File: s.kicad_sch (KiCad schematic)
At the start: 16 parts, among them J1 USB4085-GF-A_REVB, J2 UART connector, SW26 210-4MS, U1 ESP32-S3-WROOM-1, U2 MCP1825S

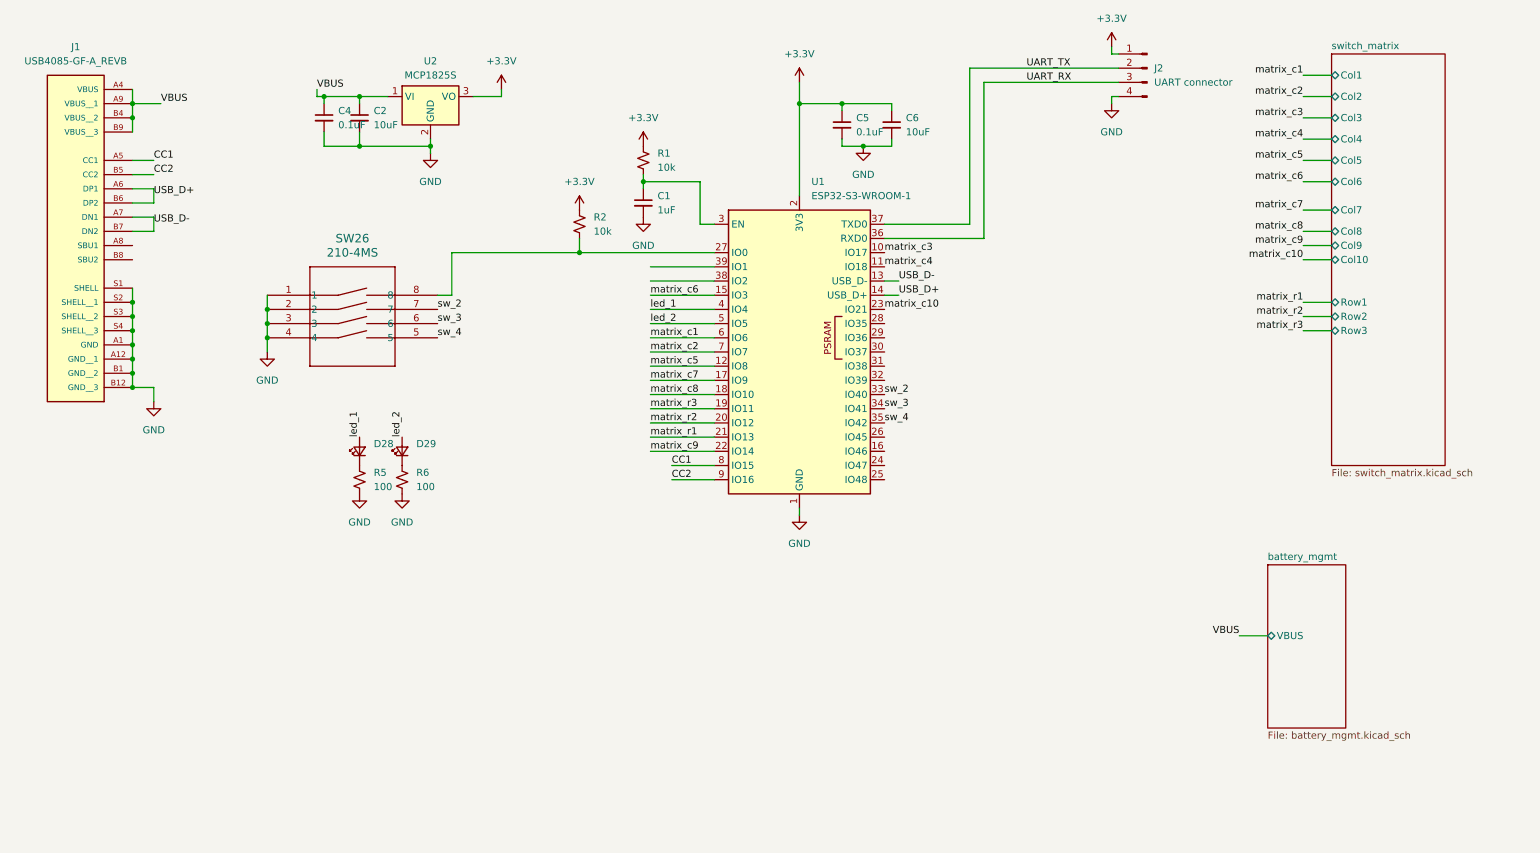
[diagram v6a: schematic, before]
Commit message: modify schematic: add switch between voltage regs
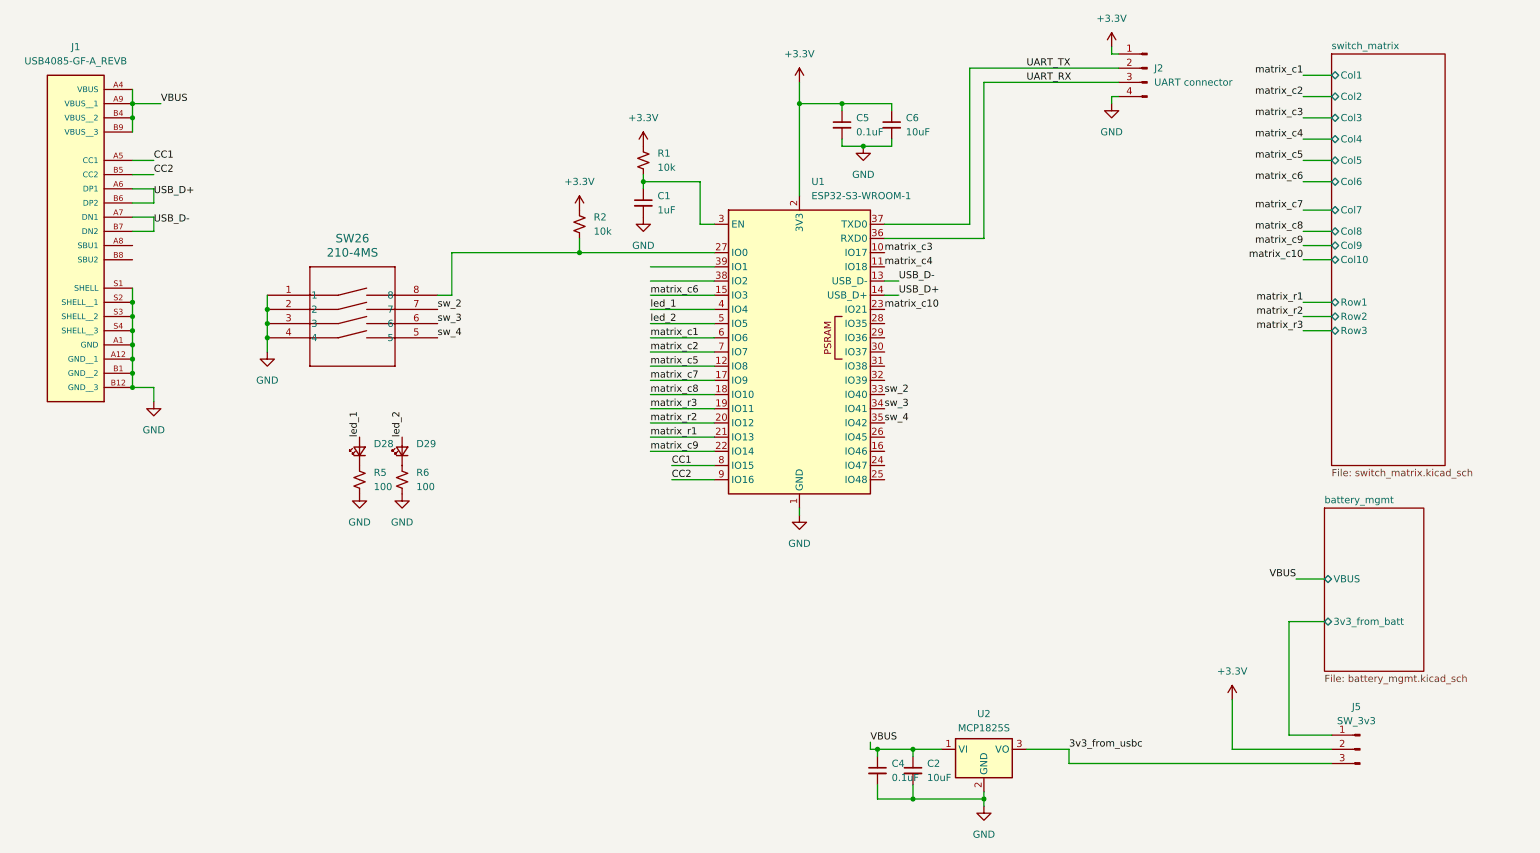
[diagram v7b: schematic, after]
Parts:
- added J5: SW_3v3, Connector_PinHeader_2.54mm:PinHeader_1x03_P2.54mm_Vertical, symbol Connector:Conn_01x03_Pin
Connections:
- net +3.3V: now also J5.2 (Pin_2); no longer U2.3 (VO)
- new net 3v3_from_usbc: J5.3 (Pin_3), U2.3 (VO)
- new net battery_mgmt/3v3_from_batt: J5.1 (Pin_1)
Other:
- sheet battery_mgmt ports: added 3v3_from_batt; removed none
- moved on the sheet: C2, C4, U2

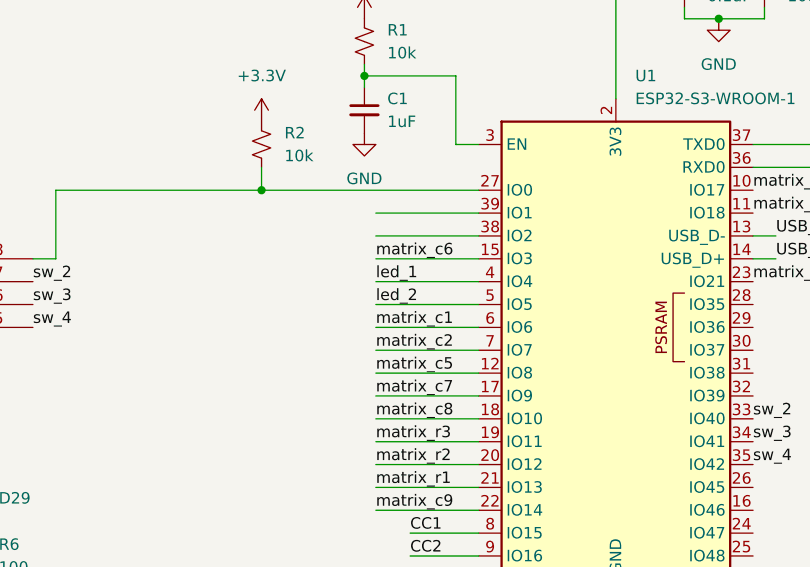
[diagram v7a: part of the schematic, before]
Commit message: more work on PCB: routed grounds
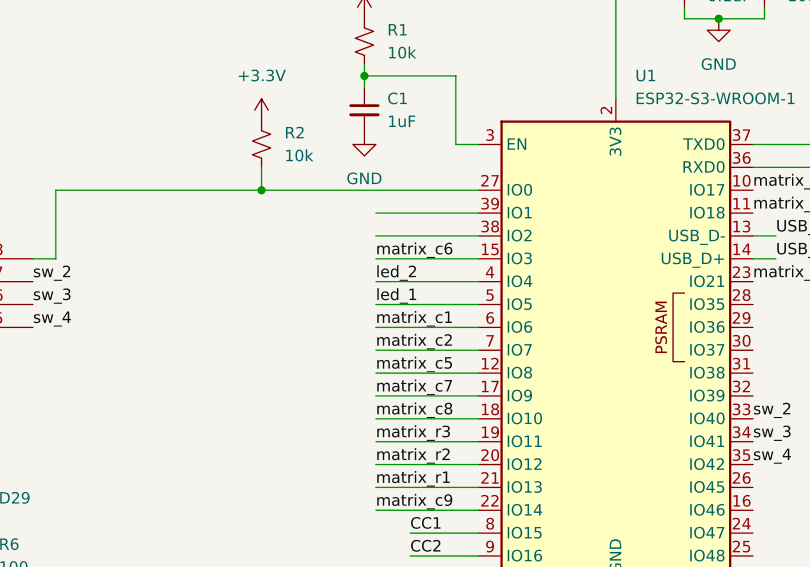
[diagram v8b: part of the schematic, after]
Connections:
- net led_1: now also U1.5 (IO5); no longer U1.4 (IO4)
- net led_2: now also U1.4 (IO4); no longer U1.5 (IO5)
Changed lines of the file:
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@@
 		)
 	)
-	(label "led_1"
+	(label "led_2"
 		(at 134.62 66.04 0)
 		(effects
@@
 		)
 	)
-	(label "led_2"
+	(label "led_1"
 		(at 134.62 68.58 0)
 		(effects
